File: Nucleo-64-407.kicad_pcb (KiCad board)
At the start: 2 copper layers, 70 x 81 mm, 72 parts, among them J1 SWD, J3 USB_B_Micro, J4 Serial 0, J5 EXP1, J6 EXP2, J7 EXP3, J8 EXP4, SW1 RESET, SW2 BOOT, U1 STM32F407VETx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

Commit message: Update a few footprints so the origin of the footpring is in teh center.
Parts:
- moved U5 14.5 mm to (65.5, 44.1)
- moved SW1 3.70 mm to (102.2, 65.5)
- moved SW2 3.70 mm to (109.8, 65.3)
- moved XS1 3.50 mm to (113.6, 43.5)
- moved J3 1.50 mm to (99.5, 37.8)

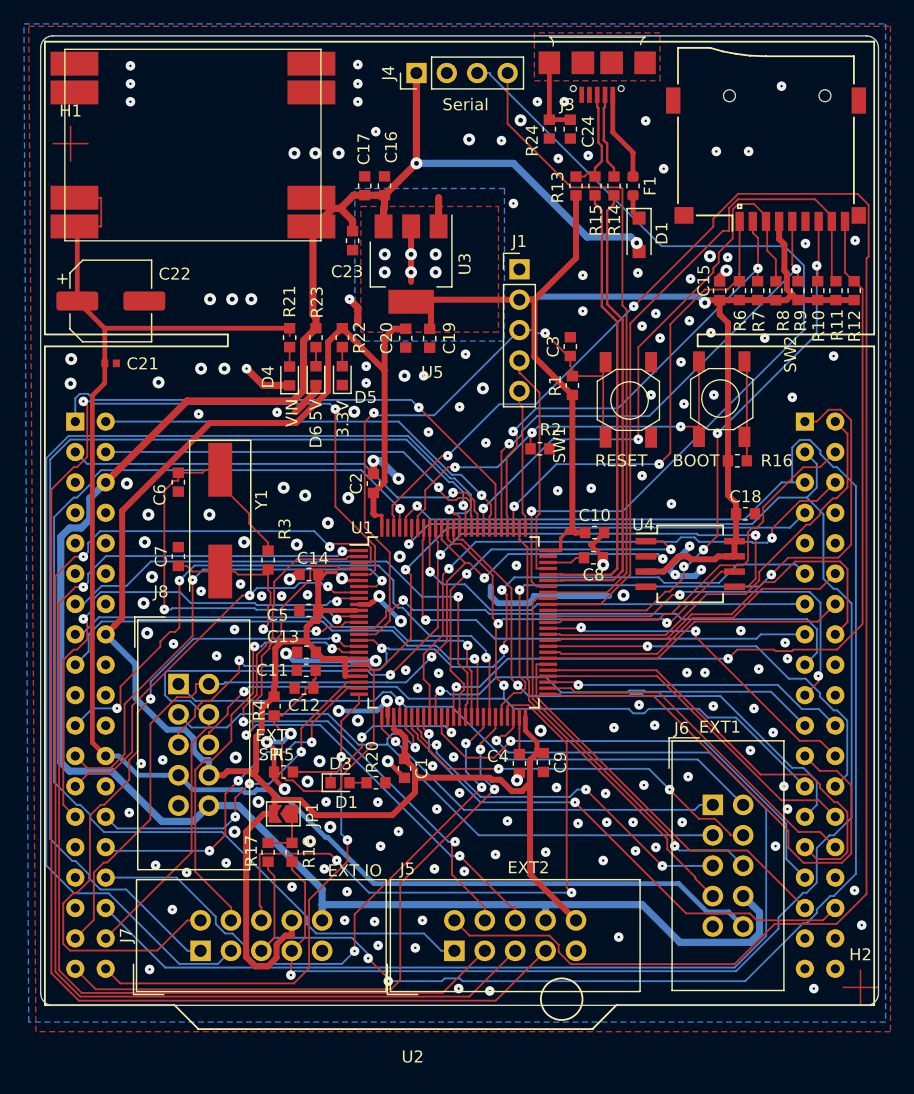
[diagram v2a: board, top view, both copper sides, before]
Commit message: Minor updates to the nucleo-64 board. Added more signals to the extension headers. Use resistor networks. Fix diode footprint.
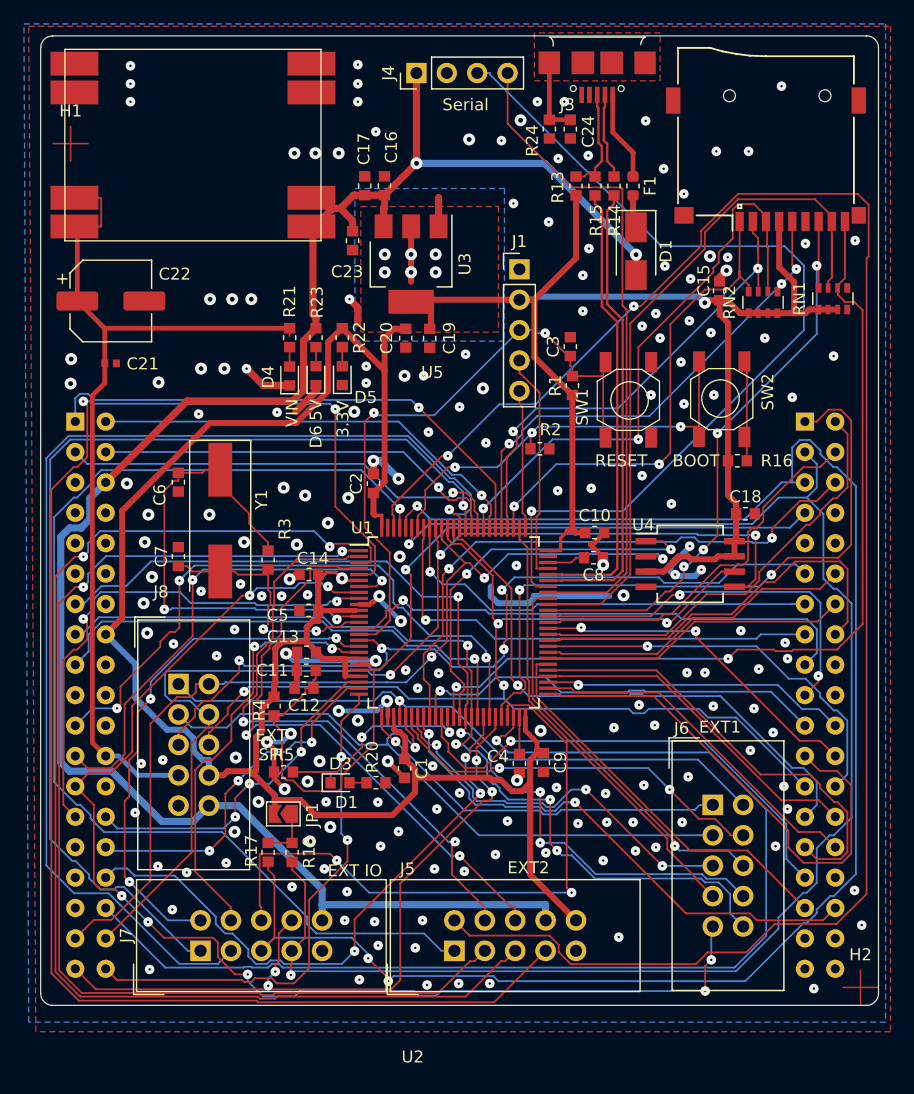
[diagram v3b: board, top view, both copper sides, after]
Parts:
- removed R10, R11, R12, R6, R7, R8, R9: 10k, PrntrBoardV1:R_0603_1608Metric
- added RN1: 4x10k, Resistor_SMD:R_Array_Convex_4x0603, F.Cu at (119.2, 57.0)
- added RN2: 4x10k, Resistor_SMD:R_Array_Convex_4x0603, F.Cu at (113.4, 57.3)
- C24: value 0.1uF -> 100nF
- D1: footprint Diode_SMD:D_SOD-123F -> Diode_SMD:D_SMA
- SW1, SW2: footprint PrntrBoardV1:Button 4x4 -> PrntrBoardV1:Button_4x4
- moved D1 1.39 mm to (102.7, 53.0)
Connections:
- J3 pad 4: Net-(J3-Pad4) -> (no net)
- J6 pad 10: /VIN -> /ENC_B
- J6 pad 8: /5V -> /ENC_A
- J6 pad 9: GND -> /BTN_IN
- J7 pad 8: /3.3V -> /~LCD_CS
- U2 pad 10: Net-(U2-Pad10) -> (no net)
- U2 pad 11: Net-(U2-Pad11) -> (no net)
- U2 pad 12: Net-(U2-Pad12) -> (no net)
- U2 pad 14: Net-(U2-Pad14) -> (no net)
- U2 pad 18: Net-(U2-Pad18) -> (no net)
- U2 pad 26: Net-(U2-Pad26) -> (no net)
- U2 pad 29: Net-(U2-Pad29) -> (no net)
- U2 pad 31: Net-(U2-Pad31) -> (no net)
- U2 pad 33: Net-(U2-Pad33) -> (no net)
- U2 pad 46: Net-(U2-Pad46) -> (no net)
- U2 pad 48: Net-(U2-Pad48) -> (no net)
- U2 pad 5: Net-(U2-Pad5) -> (no net)
- U2 pad 56: Net-(U2-Pad56) -> (no net)
- U2 pad 7: Net-(U2-Pad7) -> (no net)
- U2 pad 73: Net-(U2-Pad73) -> (no net)
- U2 pad 74: Net-(U2-Pad74) -> (no net)
- U2 pad 75: Net-(U2-Pad75) -> (no net)
- U2 pad 76: Net-(U2-Pad76) -> (no net)
- U2 pad 9: Net-(U2-Pad9) -> (no net)
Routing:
- net /BTN_IN: track 33.3 -> 104.3 mm, vias 2 -> 7
- net /VIN: track 135.1 -> 82.5 mm
- net /ENC_B: track 40.5 -> 78.2 mm, vias 1 -> 4
- net /ENC_A: track 45.1 -> 80.1 mm, vias 1 -> 4
- net /5V: track 180.0 -> 158.1 mm
- net /3.3V: track 313.5 -> 293.4 mm
- net /SPI2_MISO: track 57.2 -> 45.3 mm, vias 2 -> 3
- net /~LCD_CS: track 54.4 -> 61.5 mm, vias 2 -> 4
- net /SD_DETECT: track 73.1 -> 78.3 mm
- net /SDIO_D1: track 57.3 -> 61.2 mm
- net GND: track 68.9 -> 71.9 mm, vias 186 -> 190
- net /SDIO_D2: track 39.9 -> 41.6 mm
- net /~E0_CS: track 39.6 -> 40.9 mm
- net /IOA_7: track 31.5 -> 32.6 mm
- net /X_DIR: track 43.3 -> 44.2 mm
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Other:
- board text added: "(c) iQury.us Aug 2019"
- board text added: "BTN_IN"
- board text added: "ENC_A"
- board text added: "ENC_B"
- board text added: "Rev 3"
- board text added: "~LCD_CS"
- board text removed: "(c) iQury.us Jun 2019"
- board text removed: "Rev 4"

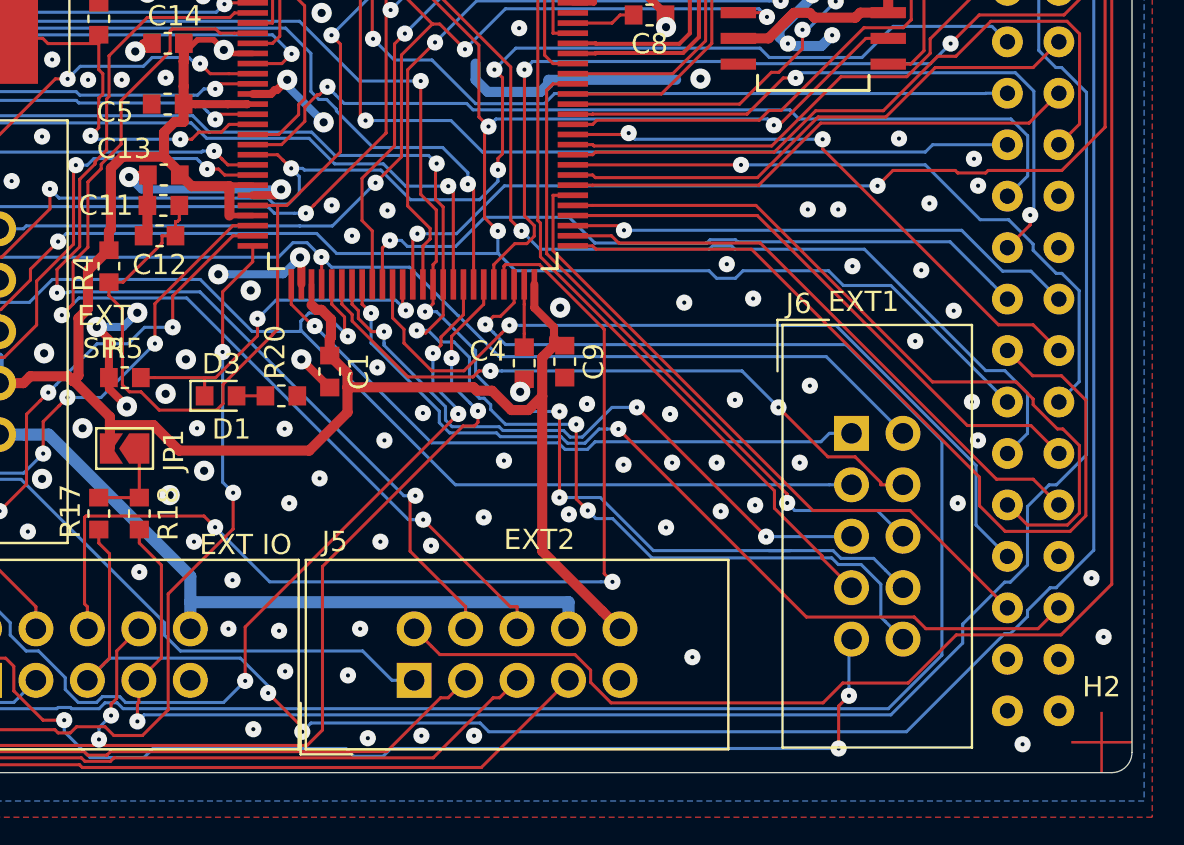
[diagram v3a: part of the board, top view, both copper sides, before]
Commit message: Add RGB leds to IO pins.
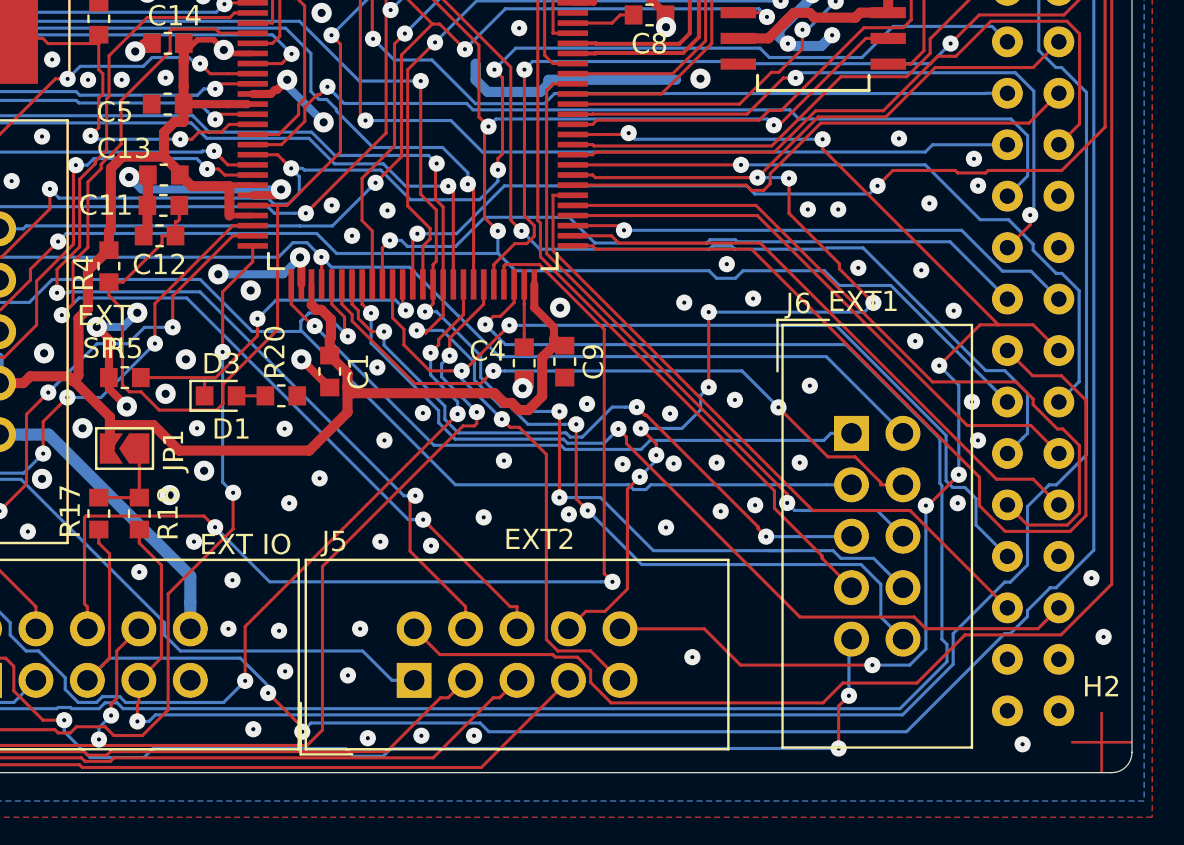
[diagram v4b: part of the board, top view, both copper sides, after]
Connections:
- J5 pad 10: /3.3V -> /~E1_CS
- J5 pad 8: /5V -> /~Z_CS
- J5 pad 9: GND -> /~E0_CS
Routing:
- net /~Z_CS: track 26.8 -> 65.5 mm, vias 0 -> 8
- net /~E1_CS: track 28.7 -> 63.8 mm, vias 2 -> 6
- net /~E0_CS: track 40.9 -> 61.0 mm, vias 1 -> 3
- net /5V: track 158.1 -> 138.1 mm
- net /3.3V: track 293.4 -> 280.3 mm
- net /BED_PWM: track 96.9 -> 97.4 mm
- net /ENC_B: track 78.2 -> 77.7 mm
- net /~Y_CS: track 25.9 -> 26.4 mm
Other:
- board text added: "BLUE ~E0_CS"
- board text added: "GREEN ~E1_CS"
- board text added: "RED ~Z_CS"

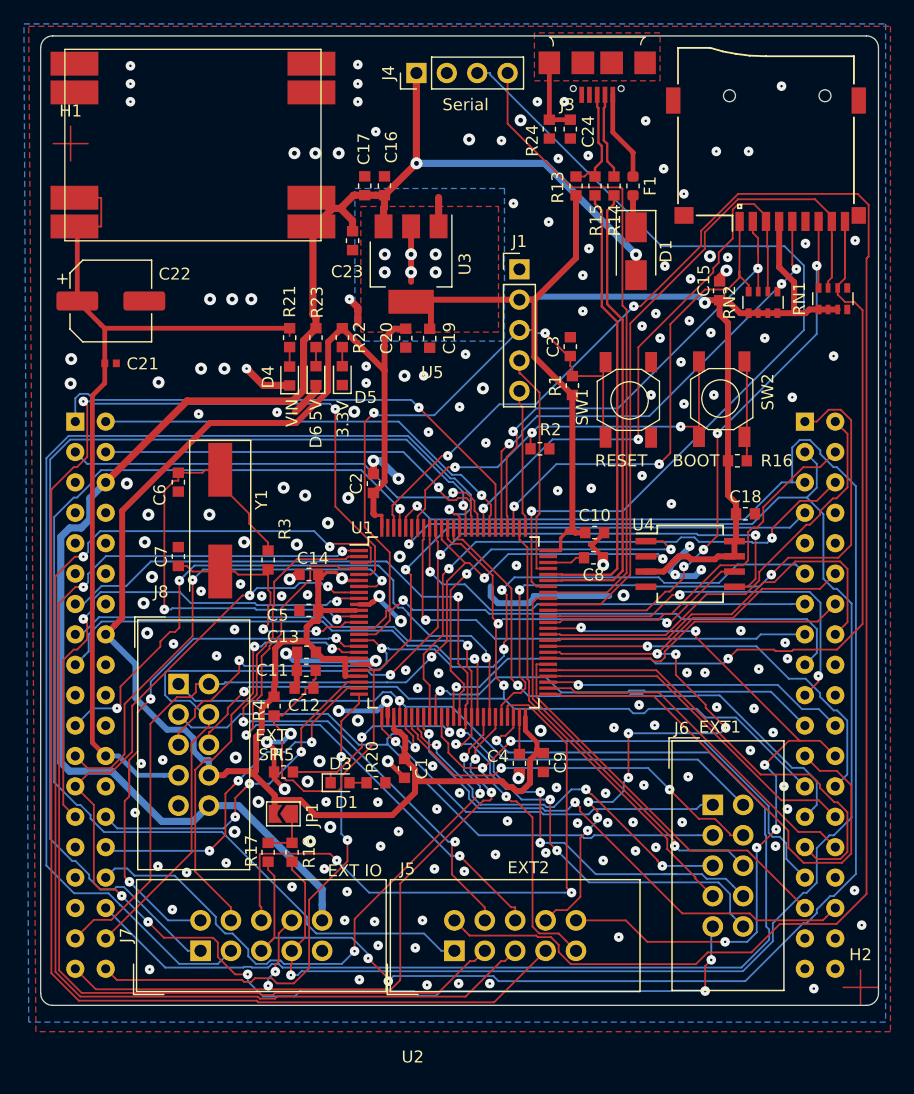
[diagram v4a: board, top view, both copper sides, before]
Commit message: Add reverse power protection to the nucleo board.
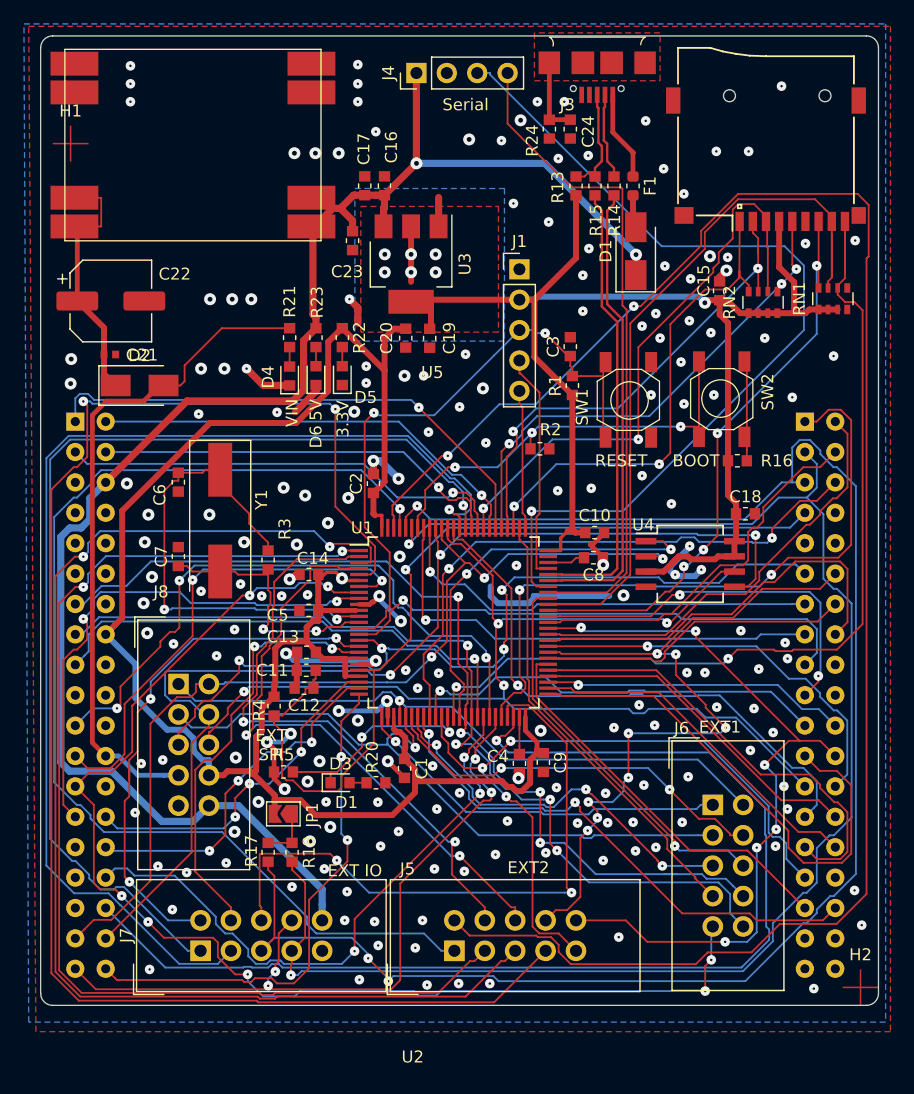
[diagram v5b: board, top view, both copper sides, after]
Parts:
- added D2: SS14, Diode_SMD:D_SMA, F.Cu at (61.3, 64.2)
- moved C21 0.74 mm to (58.8, 61.6)
- turned D1 to 90 degrees
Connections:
- C21 pad 1: /VIN -> Net-(C21-Pad1)
- C22 pad 1: /VIN -> Net-(C21-Pad1)
- D1 pad 1: Net-(D1-Pad1) -> /5V
- D1 pad 2: /5V -> Net-(D1-Pad2)
- F1 pad 2: Net-(D1-Pad1) -> Net-(D1-Pad2)
- U5 pad 1: /VIN -> Net-(C21-Pad1)
- U5 pad 2: /VIN -> Net-(C21-Pad1)
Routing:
- net Net-(C21-Pad1): track 0.00 -> 28.2 mm
- net /VIN: track 82.5 -> 56.0 mm
- net Net-(D1-Pad2): track 0.00 -> 2.77 mm
- net Net-(D1-Pad1): track 2.77 -> 0.00 mm
- net GND: vias 190 -> 189
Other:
- board text added: "(c) iQury.us Sept 2019"
- board text added: "Rev 4"
- board text removed: "(c) iQury.us Aug 2019"
- board text removed: "Rev 3"
